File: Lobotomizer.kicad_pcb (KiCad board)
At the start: 2 copper layers, 165 parts, among them J1 IN, J2 OUT, J3 Barrel_Jack, Q1 NTE467, Q2 2N5089, Q201 MPSA05, Q202 MPSA05, Q3 2N5087, Q4 2N5089, Q5 NTE467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

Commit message: finished pcb layout
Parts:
- added REF**: MountingHole_3.2mm_M3, MountingHole:MountingHole_3.2mm_M3, F.Cu at (111.8, 73.7)
- added REF**: MountingHole_3.2mm_M3, MountingHole:MountingHole_3.2mm_M3, F.Cu at (205.7, 147.3)
- added REF**: MountingHole_3.2mm_M3, MountingHole:MountingHole_3.2mm_M3, F.Cu at (205.7, 82.5)
- added REF**: MountingHole_3.2mm_M3, MountingHole:MountingHole_3.2mm_M3, F.Cu at (109.2, 144.8)
- moved C208 144.2 mm to (106.0, 80.6)
- moved C209 132.7 mm to (108.6, 87.0), turned to 180 degrees
- moved D205 122.2 mm to (94.0, 109.2)
- moved C201 98.6 mm to (158.1, 93.3), turned to 180 degrees
- moved RV204 95.9 mm to (148.6, 53.3)
- moved U202 95.8 mm to (114.3, 65.4), turned to 180 degrees
- moved R211 93.2 mm to (105.4, 54.0)
- moved RV201 87.6 mm to (176.5, 73.0), turned to 180 degrees
- moved R209 83.8 mm to (130.8, 57.1)
- moved RV205 83.0 mm to (148.6, 58.4)
- moved D206 81.6 mm to (174.6, 66.7)
- moved C202 81.3 mm to (197.5, 80.6), turned to 90 degrees
- moved R101 80.0 mm to (193.0, 124.5)
- moved R210 80.0 mm to (118.1, 54.0)
- moved R203 74.7 mm to (185.4, 77.5), turned to 180 degrees
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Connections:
- SW102 pad 1: /Lobotomizer_Reverb/BYPASS_VERB -> FUZZ_OUT
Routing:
- net VCLEAN: track 227.7 -> 404.3 mm
- net FUZZ_OUT: track 0.00 -> 118.8 mm
- net GND: track 38.5 -> 123.2 mm, vias 0 -> 20
- net Net-(C201-Pad1): track 0.00 -> 76.8 mm
- net Net-(C203-Pad2): track 0.00 -> 54.3 mm
- net Net-(R108-Pad1): track 0.00 -> 41.3 mm
- net Net-(C112-Pad1): track 0.00 -> 35.1 mm
- net Net-(C114-Pad1): track 0.00 -> 34.4 mm
- net SIGNAL_OUT: track 0.00 -> 31.6 mm
- net Net-(C106-Pad1): track 0.00 -> 27.8 mm
- net Net-(C114-Pad2): track 0.00 -> 27.4 mm
- net Net-(R114-Pad1): track 0.00 -> 27.0 mm
- net Net-(C103-Pad2): track 0.00 -> 26.8 mm
- net Net-(SW101-Pad2): track 0.00 -> 26.4 mm
- net Net-(R208-Pad1): track 0.00 -> 26.3 mm
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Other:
- board outline added: 134 x 101.6 mm

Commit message: finalized v1 design
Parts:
- added G***: LOGO, BSilk:Lobotomizer, B.Cu at (142.2, 99.1)
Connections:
- SW202 pad 2: /Lobotomizer_Saw/BYPASS_KILL -> REVERB_OUT
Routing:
- net REVERB_OUT: track 15.4 -> 60.6 mm
- net Net-(C203-Pad2): track 54.3 -> 51.0 mm
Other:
- board text added: "designed by sam blake, with much love and support from ben mcdaniels and corwin jones"

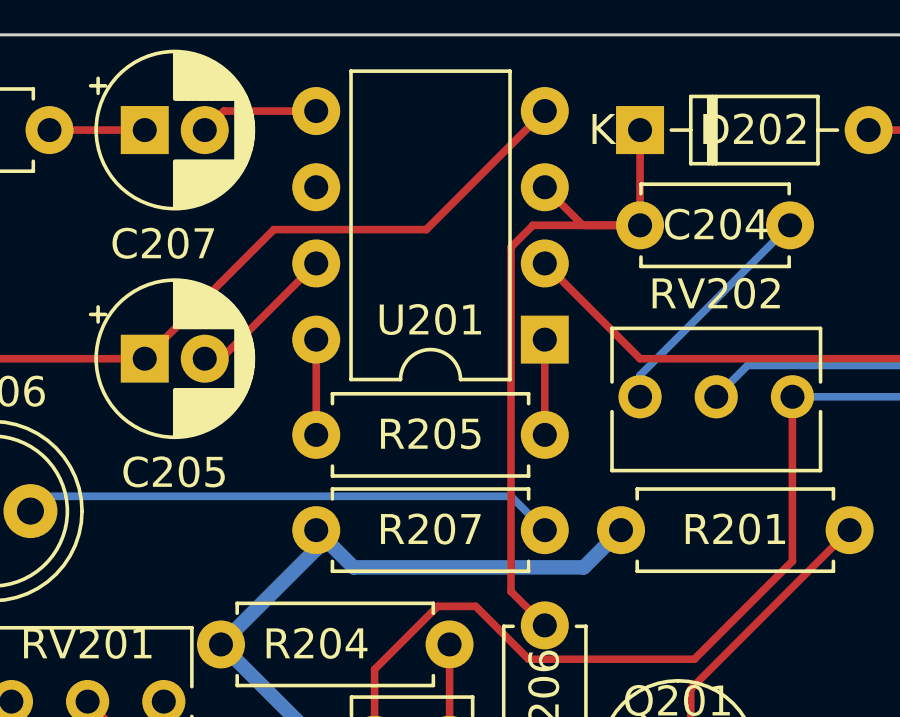
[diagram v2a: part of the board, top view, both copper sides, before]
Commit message: fixed major error
U207:7 now connected to VCLEAN.
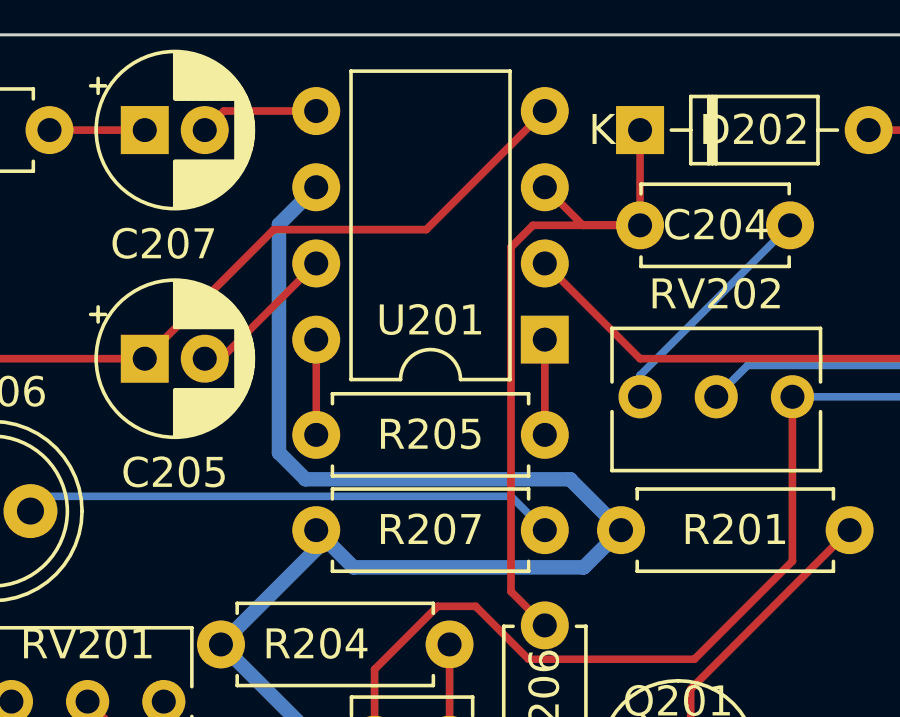
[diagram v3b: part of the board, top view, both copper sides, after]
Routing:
- net VCLEAN: track 404.3 -> 426.1 mm

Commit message: changed to pos tip, gnd sleeve jack.
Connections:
- J3 pad 1: GND -> VCLEAN
- J3 pad 2: VCLEAN -> GND
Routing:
- net GND: track 123.2 -> 129.1 mm
- net VCLEAN: track 426.1 -> 420.4 mm
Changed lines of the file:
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@@
     (thickness 1.6)
     (drawings 11)
-    (tracks 592)
+    (tracks 593)
     (zones 0)
     (modules 170)
@@
     (pad 3 thru_hole roundrect (at -3 4.7) (size 3.5 3.5) (drill oval 3 1) (layers *.Cu *.Mask) (roundrect_rratio 0.25))
     (pad 2 thru_hole roundrect (at -6 0) (size 3 3.5) (drill oval 1 3) (layers *.Cu *.Mask) (roundrect_rratio 0.25)
-      (net 32 VCLEAN))
-    (pad 1 thru_hole rect (at 0 0) (size 3.5 3.5) (drill oval 1 3) (layers *.Cu *.Mask)
       (net 1 GND))
+    (pad 1 thru_hole rect (at 0 0) (size 3.5 3.5) (drill oval 1 3) (layers *.Cu *.Mask)
+      (net 32 VCLEAN))
     (model ${KISYS3DMOD}/Connector_BarrelJack.3dshapes/BarrelJack_Horizontal.wrl
       (at (xyz 0 0 0))
@@
   (segment (start 151.765 85.725) (end 147.955 85.725) (width 0.254) (layer F.Cu) (net 1))
   (segment (start 147.955 80.645) (end 151.13 77.47) (width 0.254) (layer F.Cu) (net 1))
-  (segment (start 105.693602 99.06) (end 90.17 99.06) (width 0.254) (layer B.Cu) (net 1))
-  (segment (start 108.045 101.411398) (end 105.693602 99.06) (width 0.254) (layer B.Cu) (net 1))
   (segment (start 108.045 101.6) (end 108.045 101.411398) (width 0.254) (layer B.Cu) (net 1))
   (segment (start 173.355 61.595) (end 171.45 59.69) (width 0.254) (layer F.Cu) (net 1))
@@
   (via (at 134.62 99.06) (size 0.8) (drill 0.4) (layers F.Cu B.Cu) (net 1))
   (via (at 144.78 99.06) (size 0.8) (drill 0.4) (layers F.Cu B.Cu) (net 1))
+  (segment (start 100.058699 107.678699) (end 101.6 109.22) (width 0.4826) (layer B.Cu) (net 1))
+  (segment (start 87.477155 107.678699) (end 100.058699 107.678699) (width 0.4826) (layer B.Cu) (net 1))
+  (segment (start 84.17 104.371544) (end 87.477155 107.678699) (width 0.4826) (layer B.Cu) (net 1))
+  (segment (start 84.17 99.06) (end 84.17 104.371544) (width 0.4826) (layer B.Cu) (net 1))
   (segment (start 97.83 127) (end 91.44 127) (width 0.25) (layer F.Cu) (net 2))
   (segment (start 104.14 127) (end 100.33 127) (width 0.25) (layer F.Cu) (net 3))
@@
   (segment (start 118.138699 128.230825) (end 121.324175 131.416301) (width 0.4826) (layer F.Cu) (net 32))
   (segment (start 104.14 119.38) (end 106.651301 116.868699) (width 0.4826) (layer F.Cu) (net 32))
-  (segment (start 86.67869 101.56869) (end 84.17 99.06) (width 0.4826) (layer F.Cu) (net 32))
-  (segment (start 88.590234 101.56869) (end 86.67869 101.56869) (width 0.4826) (layer F.Cu) (net 32))
   (segment (start 165.733427 139.769447) (end 165.733427 141.671301) (width 0.4826) (layer B.Cu) (net 32))
   (segment (start 175.895 129.607874) (end 165.733427 139.769447) (width 0.4826) (layer B.Cu) (net 32))
   (segment (start 175.895 123.19) (end 175.895 129.607874) (width 0.4826) (layer B.Cu) (net 32))
   (segment (start 93.94869 101.56869) (end 93.98 101.6) (width 0.4826) (layer F.Cu) (net 32))
-  (segment (start 88.590234 101.56869) (end 93.94869 101.56869) (width 0.4826) (layer F.Cu) (net 32))
   (segment (start 93.98 101.6) (end 93.98 105.41) (width 0.4826) (layer F.Cu) (net 32))
   (segment (start 101.6 101.6) (end 101.6 105.41) (width 0.4826) (layer F.Cu) (net 32))
@@
   (segment (start 185.448699 57.121301) (end 185.448699 64.730825) (width 0.4826) (layer B.Cu) (net 32))
   (segment (start 186.69 55.88) (end 185.448699 57.121301) (width 0.4826) (layer B.Cu) (net 32))
+  (segment (start 91.906289 101.6) (end 89.768145 99.461856) (width 0.4826) (layer B.Cu) (net 32))
+  (segment (start 93.98 101.6) (end 91.906289 101.6) (width 0.4826) (layer B.Cu) (net 32))
   (segment (start 157.644999 140.170001) (end 154.94 142.875) (width 0.4826) (layer F.Cu) (net 33))
   (segment (start 157.644999 132.879999) (end 157.644999 140.170001) (width 0.4826) (layer F.Cu) (net 33))
